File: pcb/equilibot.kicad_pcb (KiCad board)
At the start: 4 copper layers, 155 parts, among them IC1 TMC5240, IC2 TMC5240, IC3 TPS561243DRLR, IC4 TPS561243DRLR, J1 Conn_01x02_Socket, J10 Conn_01x02_Socket, J11 Conn_01x02_Pin, J12 Conn_01x02_Socket, J2 USB_C_Receptacle_USB2.0_16P, J3 Conn_01x04_Pin, J4 Conn_01x04_Pin, J5 Conn_01x03_Pin, J6 Conn_01x03_Socket, J7 Conn_01x08_Pin, J8 Conn_01x08_Socket, J9 Conn_01x02_Pin, SW1 SW_Push, SW2 SW_Push, U1 ESP32-S3-WROOM-1, U2 SN74LVC1T45DBV, U3 USBLC6-2P6, U4 XC6206PxxxMR

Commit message: routing
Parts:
- removed C43, C44, C45, C46, C47, C49, C50: 100n, Capacitor_SMD:C_0603_1608Metric
- removed D32, D33, D34, D35, D36: WS2812B, Equilibot:XL_WS2812B_1615
- removed J10, J12: Conn_01x02_Socket, Connector_PinSocket_2.54mm:PinSocket_1x02_P2.54mm_Vertical
- removed J11, J9: Conn_01x02_Pin, Connector_PinSocket_2.54mm:PinSocket_1x02_P2.54mm_Vertical
- removed J6: Conn_01x03_Socket, Connector_PinSocket_2.54mm:PinSocket_1x03_P2.54mm_Vertical
- removed J8: Conn_01x08_Socket, Connector_PinSocket_2.54mm:PinSocket_2x04_P2.54mm_Vertical
- removed R11, R8: 5.1k, Resistor_SMD:R_0603_1608Metric
- added TP10: TestPoint, TestPoint:TestPoint_Pad_D1.0mm, F.Cu at (140.2, 89.6)
- added TP11: TestPoint, Equilibot:TestPoint_Pad_1.0x1.0mm, B.Cu at (165.4, 108.4)
- added TP12: TestPoint, Equilibot:TestPoint_Pad_1.0x1.0mm, F.Cu at (182.0, 83.0)
- added TP13: TestPoint, Equilibot:TestPoint_Pad_1.0x1.0mm, F.Cu at (180.6, 80.0)
- added TP14: TestPoint, Equilibot:TestPoint_Pad_1.0x1.0mm, F.Cu at (179.1, 83.0)
- added TP15: TestPoint, Equilibot:TestPoint_Pad_1.0x1.0mm, F.Cu at (177.8, 80.0)
- added TP17: TestPoint, Equilibot:TestPoint_Pad_1.0x1.0mm, F.Cu at (183.4, 80.0)
- added TP18: TestPoint, Equilibot:TestPoint_Pad_1.0x1.0mm, F.Cu at (176.3, 83.0)
- added TP19: TestPoint, Equilibot:TestPoint_Pad_1.0x1.0mm, F.Cu at (173.4, 83.0)
- added TP20: TestPoint, Equilibot:TestPoint_Pad_1.0x1.0mm, F.Cu at (174.9, 80.0)
- added TP9: TestPoint, TestPoint:TestPoint_Pad_D1.0mm, F.Cu at (146.4, 96.6)
- C10, C18, C19, C20, C21, C7, C8, C9: footprint Capacitor_SMD:C_0805_2012Metric -> Capacitor_SMD:C_0603_1608Metric
- C39, C40, C41, C42, C48, J7: moved to B.Cu
- J1: footprint Connector_AMASS:AMASS_XT60-M_1x02_P7.20mm_Vertical -> Connector_AMASS:AMASS_XT60PW-M_1x02_P7.20mm_Horizontal
- J2: footprint Connector_USB:USB_C_Receptacle_GCT_USB4105-xx-A_16P_TopMnt_Horizontal -> Equilibot:USB_C_Receptacle_GCT_USB4105-xx-A_16P_TopMnt_Horizontal
- MT1: footprint ICM-42670-P:XDCR_ICM-42670-P -> Equilibot:XDCR_ICM-42670-P
- SW1, SW2: footprint Button_Switch_SMD:SW_SPST_TL3342 -> Connector_PinHeader_2.54mm:PinHeader_1x02_P2.54mm_Vertical; moved to B.Cu
- TP1, TP2, TP3, TP7: footprint TestPoint:TestPoint_Plated_Hole_D2.0mm -> TestPoint:TestPoint_Pad_D1.0mm
- TP16, TP8: footprint TestPoint:TestPoint_Pad_D1.0mm -> Equilibot:TestPoint_Pad_1.0x1.0mm; moved to B.Cu
- U1: footprint RF_Module:ESP32-S3-WROOM-1 -> Equilibot:ESP32-S3-WROOM-1
- moved D1 85.5 mm to (163.5, 110.5)
- moved D2 85.1 mm to (163.7, 108.2), turned to -10 degrees
- moved D3 84.0 mm to (164.3, 106.1), turned to -20 degrees
- moved D4 82.1 mm to (165.2, 104.0), turned to -30 degrees
- moved D5 79.6 mm to (166.5, 102.1), turned to -40 degrees
- moved D6 76.5 mm to (168.1, 100.5), turned to -50 degrees
- moved D7 73.0 mm to (170.0, 99.2), turned to -60 degrees
- moved D8 69.0 mm to (172.1, 98.3), turned to -70 degrees
- moved C40 67.8 mm to (176.4, 100.9), turned to 0 degrees
- moved TP3 65.2 mm to (157.6, 75.4), turned to 90 degrees
- moved C41 64.9 mm to (182.0, 101.5), turned to 0 degrees
- moved D9 64.8 mm to (174.2, 97.7), turned to -80 degrees
- moved TP7 64.7 mm to (157.6, 81.0), turned to 90 degrees
- moved D27 64.3 mm to (172.5, 105.5), turned to -90 degrees
- moved D26 64.1 mm to (170.5, 105.5), turned to -90 degrees
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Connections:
- C32 pad 2: /psu/SW -> /psu/SW3V3
- C37 pad 2: /psu/SW -> /psu/SW5V
- C4 pad 1: Net-(C4-Pad1) -> GND
- C5 pad 1: Net-(C4-Pad1) -> GND
- C6 pad 2: unconnected-(C6-Pad2) -> GND
- D31 pad 4: Net-(D31-DOUT) -> unconnected-(D31-DOUT-Pad4)
- IC3 pad 4: /psu/SW -> /psu/SW3V3
- IC4 pad 4: /psu/SW -> /psu/SW5V
- J7 pad 1: /3V3 -> /SPI_CS_IMU
- J7 pad 2: /IMU_INT1 -> /SPI_SCLK
- J7 pad 3: /IMU_INT2 -> /SPI_MOSI
- J7 pad 4: /SPI_CS_IMU -> /SPI_MISO
- J7 pad 5: /SPI_MISO -> /IMU_INT2
- J7 pad 6: /SPI_MOSI -> /IMU_INT1
- J7 pad 7: /SPI_SCLK -> /3V3
- MT1 pad 1: /SPI_SCLK -> /SPI_MISO
- MT1 pad 13: /SPI_MISO -> /SPI_SCLK
- U1 pad 21: /SPI_SCLK -> /SPI_MISO
- U1 pad 23: /SPI_MISO -> /SPI_SCLK
- U1 pad 32: unconnected-(U1-IO39-Pad32) -> /SPI_CS_IMU
- U1 pad 33: unconnected-(U1-IO40-Pad33) -> /IMU_INT2
- U1 pad 34: unconnected-(U1-IO41-Pad34) -> /IMU_INT1
- U1 pad 5: /SPI_CS_IMU -> unconnected-(U1-IO5-Pad5)
- U1 pad 6: /IMU_INT1 -> unconnected-(U1-IO6-Pad6)
- U1 pad 7: /IMU_INT2 -> unconnected-(U1-IO7-Pad7)
- U3 pad 1: /USB_N -> /USB_P
- U3 pad 3: /USB_P -> /USB_N
- U3 pad 4: Net-(J2-D+-PadA6) -> Net-(J2-D--PadA7)
- U3 pad 6: Net-(J2-D--PadA7) -> Net-(J2-D+-PadA6)
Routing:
- net /5V: track 0.00 -> 142.1 mm, vias 0 -> 12
- net /VM: track 0.00 -> 133.7 mm, vias 0 -> 2
- net /3V3: track 0.00 -> 106.2 mm, vias 0 -> 8
- net /SPI_SCLK: track 0.00 -> 99.0 mm, vias 0 -> 6
- net /SPI_MISO: track 0.00 -> 95.2 mm, vias 0 -> 6
- net /SPI_MOSI: track 0.00 -> 92.8 mm, vias 0 -> 7
- net /IMU_INT1: track 0.00 -> 51.9 mm, vias 0 -> 3
- net /SPI_CS_IMU: track 0.00 -> 50.2 mm, vias 0 -> 3
- net GND: track 0.00 -> 49.2 mm, vias 98 -> 90
- net /IMU_INT2: track 0.00 -> 38.6 mm, vias 0 -> 2
- net /SPI_CS_STP1: track 0.00 -> 37.2 mm, vias 0 -> 2
- net Net-(R1-Pad1): track 0.00 -> 33.6 mm, vias 0 -> 1
- net /STP1_DRV_EN: track 0.00 -> 25.9 mm, vias 0 -> 2
- net /leds/DIN_5V: track 0.00 -> 24.3 mm, vias 0 -> 1
- net /SPI_CS_STP2: track 0.00 -> 24.1 mm, vias 0 -> 2
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- added copper zone on In1.Cu, net GND
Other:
- board outline added: 88.3 x 49.5 mm

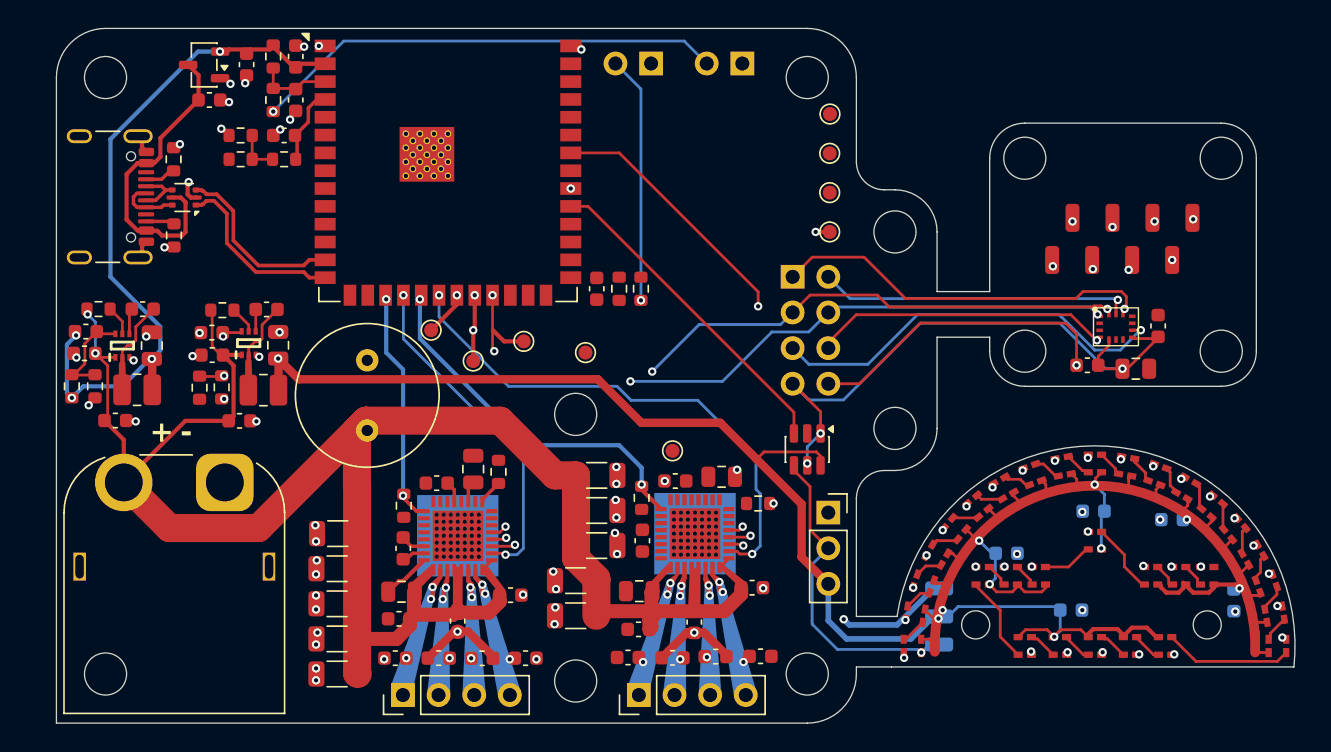
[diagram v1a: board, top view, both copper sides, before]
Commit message: add jlcpcb part numbers
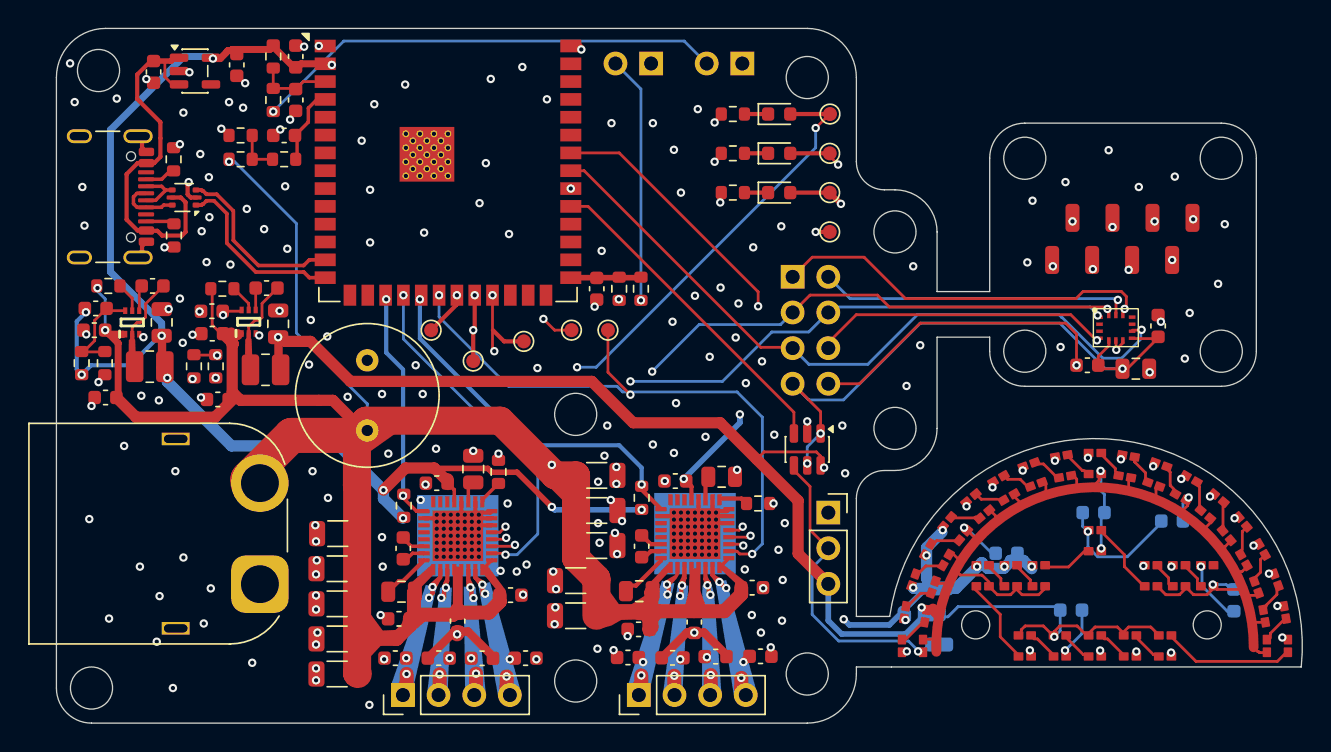
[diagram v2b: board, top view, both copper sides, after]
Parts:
- added D32: LED_Small, LED_SMD:LED_0603_1608Metric, F.Cu at (154.0, 72.6)
- added D33: LED_Small, LED_SMD:LED_0603_1608Metric, F.Cu at (154.0, 75.4)
- added D34: LED_Small, LED_SMD:LED_0603_1608Metric, F.Cu at (154.0, 78.2)
- added R11: 3k, Resistor_SMD:R_0603_1608Metric, F.Cu at (150.7, 75.4)
- added R22: 1k, Resistor_SMD:R_0603_1608Metric, F.Cu at (150.7, 78.2)
- added R8: 10k, Resistor_SMD:R_0603_1608Metric, F.Cu at (150.7, 72.6)
- C10, C18, C19, C20, C21, C7, C8, C9: value 220p -> 470p
- C17, C34: value 2.7u -> 2.2u
- C27, C64: value 22u -> 10u
- C3, C30, C35, C4, C6: value 100n -> 220n
- D1, D10, D11, D12, D13, D14, D15, D16, D17, D18, D19, D2, D20, D21, D22, D23, D24, D25, D26, D27, D28, D29, D3, D30, D31, D4, D5, D6, D7, D8, D9: footprint Equilibot:XL_WS2812B_1615 -> Equilibot:XL_WS2812B_0807
- U4: value XC6206PxxxMR -> TLV75533PDBV; footprint Package_TO_SOT_SMD:SOT-23-3 -> Package_TO_SOT_SMD:SOT-23-5
- moved TP9 11.2 mm to (139.2, 88.0)
- moved J1 7.67 mm to (117.0, 106.1), turned to 90 degrees
- moved C40 5.64 mm to (182.0, 101.6)
- moved C41 5.62 mm to (176.4, 101.0)
- moved C51 4.45 mm to (109.4, 69.6), turned to 90 degrees
- moved TP10 2.26 mm to (141.8, 88.0)
- moved C27 2.17 mm to (114.0, 92.9), turned to 180 degrees
- moved L1 1.88 mm to (109.2, 90.6)
- moved C30 1.79 mm to (105.2, 88.0)
- moved R13 1.79 mm to (106.2, 84.8)
- moved R14 1.79 mm to (104.3, 90.3)
- moved R15 1.79 mm to (106.0, 90.3)
- moved C32 1.79 mm to (109.3, 84.8)
- moved C31 1.79 mm to (110.0, 87.5)
- moved C33 1.79 mm to (105.3, 86.5)
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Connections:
- D1 pad 1: GND -> Net-(D1-DOUT)
- D1 pad 2: /leds/DIN_5V -> GND
- D1 pad 3: /5V -> /leds/DIN_5V
- D1 pad 4: Net-(D1-DOUT) -> /5V
- D10 pad 1: GND -> Net-(D10-DOUT)
- D10 pad 2: Net-(D10-DIN) -> GND
- D10 pad 3: /5V -> Net-(D10-DIN)
- D10 pad 4: Net-(D10-DOUT) -> /5V
- D11 pad 1: GND -> Net-(D11-DOUT)
- D11 pad 2: Net-(D10-DOUT) -> GND
- D11 pad 3: /5V -> Net-(D10-DOUT)
- D11 pad 4: Net-(D11-DOUT) -> /5V
- D12 pad 1: GND -> /leds/O1
- D12 pad 2: Net-(D11-DOUT) -> GND
- D12 pad 3: /5V -> Net-(D11-DOUT)
- D12 pad 4: /leds/O1 -> /5V
- D13 pad 1: GND -> Net-(D13-DOUT)
- D13 pad 2: /leds/O1 -> GND
- D13 pad 3: /5V -> /leds/O1
- D13 pad 4: Net-(D13-DOUT) -> /5V
- D14 pad 1: GND -> Net-(D14-DOUT)
- D14 pad 2: Net-(D13-DOUT) -> GND
- D14 pad 3: /5V -> Net-(D13-DOUT)
- D14 pad 4: Net-(D14-DOUT) -> /5V
- D15 pad 1: GND -> Net-(D15-DOUT)
- D15 pad 2: Net-(D14-DOUT) -> GND
- D15 pad 3: /5V -> Net-(D14-DOUT)
- D15 pad 4: Net-(D15-DOUT) -> /5V
- D16 pad 1: GND -> Net-(D16-DOUT)
- D16 pad 2: Net-(D15-DOUT) -> GND
- D16 pad 3: /5V -> Net-(D15-DOUT)
- D16 pad 4: Net-(D16-DOUT) -> /5V
- D17 pad 1: GND -> Net-(D17-DOUT)
- D17 pad 2: Net-(D16-DOUT) -> GND
- D17 pad 3: /5V -> Net-(D16-DOUT)
- D17 pad 4: Net-(D17-DOUT) -> /5V
- D18 pad 1: GND -> Net-(D18-DOUT)
- D18 pad 2: Net-(D17-DOUT) -> GND
- D18 pad 3: /5V -> Net-(D17-DOUT)
- D18 pad 4: Net-(D18-DOUT) -> /5V
- D19 pad 1: GND -> Net-(D19-DOUT)
- D19 pad 2: Net-(D18-DOUT) -> GND
- D19 pad 3: /5V -> Net-(D18-DOUT)
- D19 pad 4: Net-(D19-DOUT) -> /5V
- D2 pad 1: GND -> Net-(D2-DOUT)
- D2 pad 2: Net-(D1-DOUT) -> GND
- D2 pad 3: /5V -> Net-(D1-DOUT)
- D2 pad 4: Net-(D2-DOUT) -> /5V
- D20 pad 1: GND -> Net-(D20-DOUT)
- D20 pad 2: Net-(D19-DOUT) -> GND
- D20 pad 3: /5V -> Net-(D19-DOUT)
- D20 pad 4: Net-(D20-DOUT) -> /5V
- D21 pad 1: GND -> Net-(D21-DOUT)
- D21 pad 2: Net-(D20-DOUT) -> GND
- D21 pad 3: /5V -> Net-(D20-DOUT)
- D21 pad 4: Net-(D21-DOUT) -> /5V
- D22 pad 1: GND -> Net-(D22-DOUT)
- D22 pad 2: Net-(D21-DOUT) -> GND
- D22 pad 3: /5V -> Net-(D21-DOUT)
- D22 pad 4: Net-(D22-DOUT) -> /5V
- D23 pad 1: GND -> Net-(D23-DOUT)
- D23 pad 2: Net-(D22-DOUT) -> GND
- D23 pad 3: /5V -> Net-(D22-DOUT)
- D23 pad 4: Net-(D23-DOUT) -> /5V
- D24 pad 1: GND -> /leds/O2
- D24 pad 2: Net-(D23-DOUT) -> GND
- D24 pad 3: /5V -> Net-(D23-DOUT)
- D24 pad 4: /leds/O2 -> /5V
- D25 pad 1: GND -> Net-(D25-DOUT)
- D25 pad 2: /leds/O2 -> GND
- D25 pad 3: /5V -> /leds/O2
- D25 pad 4: Net-(D25-DOUT) -> /5V
- D26 pad 1: GND -> Net-(D26-DOUT)
- D26 pad 2: Net-(D25-DOUT) -> GND
- D26 pad 3: /5V -> Net-(D25-DOUT)
- D26 pad 4: Net-(D26-DOUT) -> /5V
- D27 pad 1: GND -> Net-(D27-DOUT)
- D27 pad 2: Net-(D26-DOUT) -> GND
- D27 pad 3: /5V -> Net-(D26-DOUT)
- D27 pad 4: Net-(D27-DOUT) -> /5V
- D28 pad 1: GND -> Net-(D28-DOUT)
- D28 pad 2: Net-(D27-DOUT) -> GND
- D28 pad 3: /5V -> Net-(D27-DOUT)
- D28 pad 4: Net-(D28-DOUT) -> /5V
- D29 pad 1: GND -> Net-(D29-DOUT)
- D29 pad 2: Net-(D28-DOUT) -> GND
- D29 pad 3: /5V -> Net-(D28-DOUT)
- D29 pad 4: Net-(D29-DOUT) -> /5V
- D3 pad 1: GND -> Net-(D3-DOUT)
- D3 pad 2: Net-(D2-DOUT) -> GND
- D3 pad 3: /5V -> Net-(D2-DOUT)
- D3 pad 4: Net-(D3-DOUT) -> /5V
- D30 pad 1: GND -> Net-(D30-DOUT)
- D30 pad 2: Net-(D29-DOUT) -> GND
- D30 pad 3: /5V -> Net-(D29-DOUT)
- D30 pad 4: Net-(D30-DOUT) -> /5V
- D31 pad 1: GND -> unconnected-(D31-DOUT-Pad1)
- D31 pad 2: Net-(D30-DOUT) -> GND
- D31 pad 3: /5V -> Net-(D30-DOUT)
- D31 pad 4: unconnected-(D31-DOUT-Pad4) -> /5V
- D4 pad 1: GND -> Net-(D4-DOUT)
- D4 pad 2: Net-(D3-DOUT) -> GND
- D4 pad 3: /5V -> Net-(D3-DOUT)
- D4 pad 4: Net-(D4-DOUT) -> /5V
- D5 pad 1: GND -> Net-(D5-DOUT)
- D5 pad 2: Net-(D4-DOUT) -> GND
- D5 pad 3: /5V -> Net-(D4-DOUT)
- D5 pad 4: Net-(D5-DOUT) -> /5V
- D6 pad 1: GND -> Net-(D6-DOUT)
- D6 pad 2: Net-(D5-DOUT) -> GND
- D6 pad 3: /5V -> Net-(D5-DOUT)
- D6 pad 4: Net-(D6-DOUT) -> /5V
- D7 pad 1: GND -> Net-(D7-DOUT)
- D7 pad 2: Net-(D6-DOUT) -> GND
- D7 pad 3: /5V -> Net-(D6-DOUT)
- D7 pad 4: Net-(D7-DOUT) -> /5V
- D8 pad 1: GND -> Net-(D8-DOUT)
- D8 pad 2: Net-(D7-DOUT) -> GND
- D8 pad 3: /5V -> Net-(D7-DOUT)
- D8 pad 4: Net-(D8-DOUT) -> /5V
- D9 pad 1: GND -> Net-(D10-DIN)
- D9 pad 2: Net-(D8-DOUT) -> GND
- D9 pad 3: /5V -> Net-(D8-DOUT)
- D9 pad 4: Net-(D10-DIN) -> /5V
- U1 pad 41: Net-(U1-GND-Pad40) -> GND
- U4 pad 1: GND -> Net-(U3-VBUS)
- U4 pad 2: /3V3 -> GND
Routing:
- net /3V3: track 106.2 -> 218.7 mm, vias 8 -> 18
- net /VM: track 133.7 -> 186.3 mm, vias 2 -> 6
- net GND: track 49.2 -> 94.0 mm, vias 90 -> 217
- net /5V: track 142.1 -> 174.5 mm
- net /IMU_INT2: track 38.6 -> 60.3 mm
- net /SPI_CS_STP2: track 24.1 -> 39.2 mm, vias 2 -> 3
- net /SPI_CS_STP1: track 37.2 -> 44.6 mm, vias 2 -> 3
- net Net-(U1-IO0): track 0.00 -> 5.03 mm
- net Net-(U3-VBUS): track 22.0 -> 25.7 mm
- net Net-(IC2-VCP): track 0.00 -> 3.09 mm
- net Net-(IC2-IREF): track 0.00 -> 2.02 mm
- net /leds/DIN_5V: track 24.3 -> 22.2 mm
- net Net-(D32-K): track 0.00 -> 1.95 mm
- net Net-(IC2-VDD_1V8): track 0.00 -> 1.79 mm
- net Net-(D34-K): track 0.00 -> 1.65 mm
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- added copper zone on In2.Cu, net GND
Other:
- board size 88.3 x 49.5 mm -> 88.8 x 49.5 mm
